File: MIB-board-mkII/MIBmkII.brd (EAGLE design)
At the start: 68.2 x 43.2 mm, 27 parts, among them IC1 74HC125N, X1 MAB5SH, X2 MAB5SH

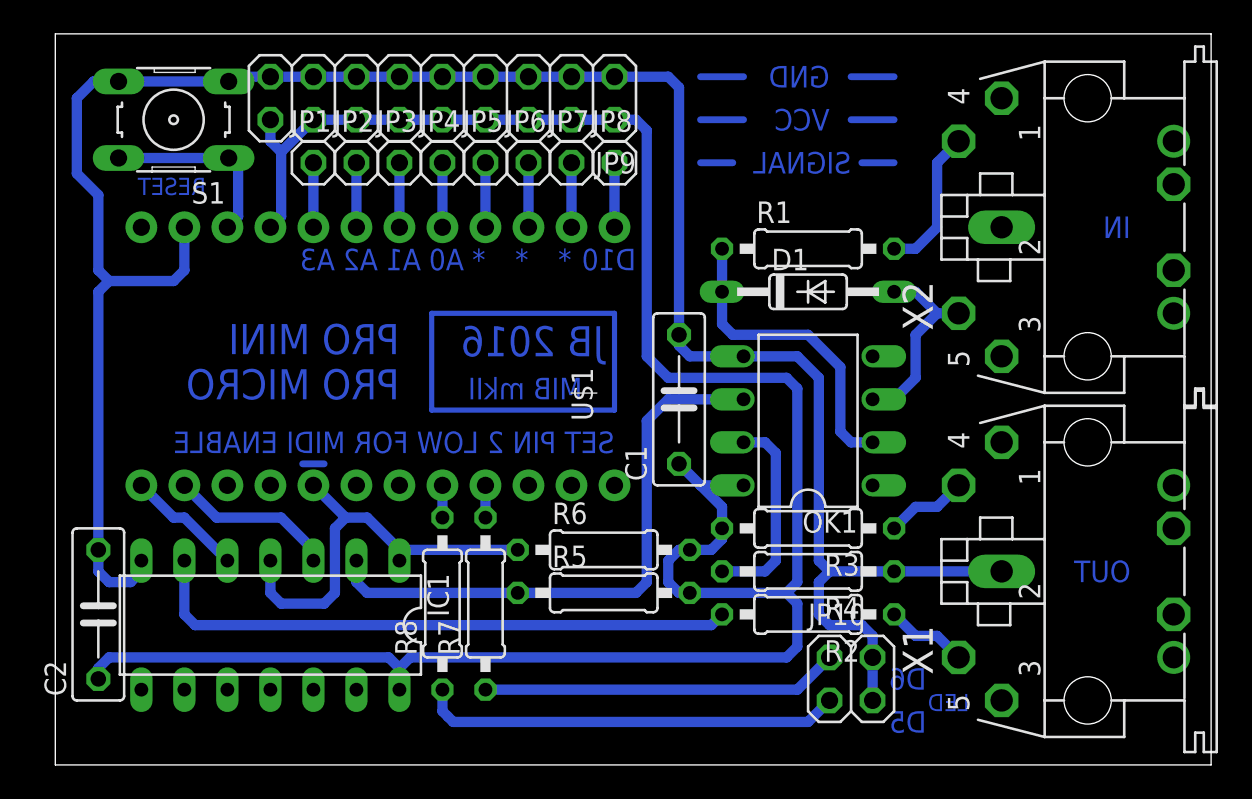
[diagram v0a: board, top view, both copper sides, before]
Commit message: Corrected labeling on silkscreen. Increased size of some pads and traces.
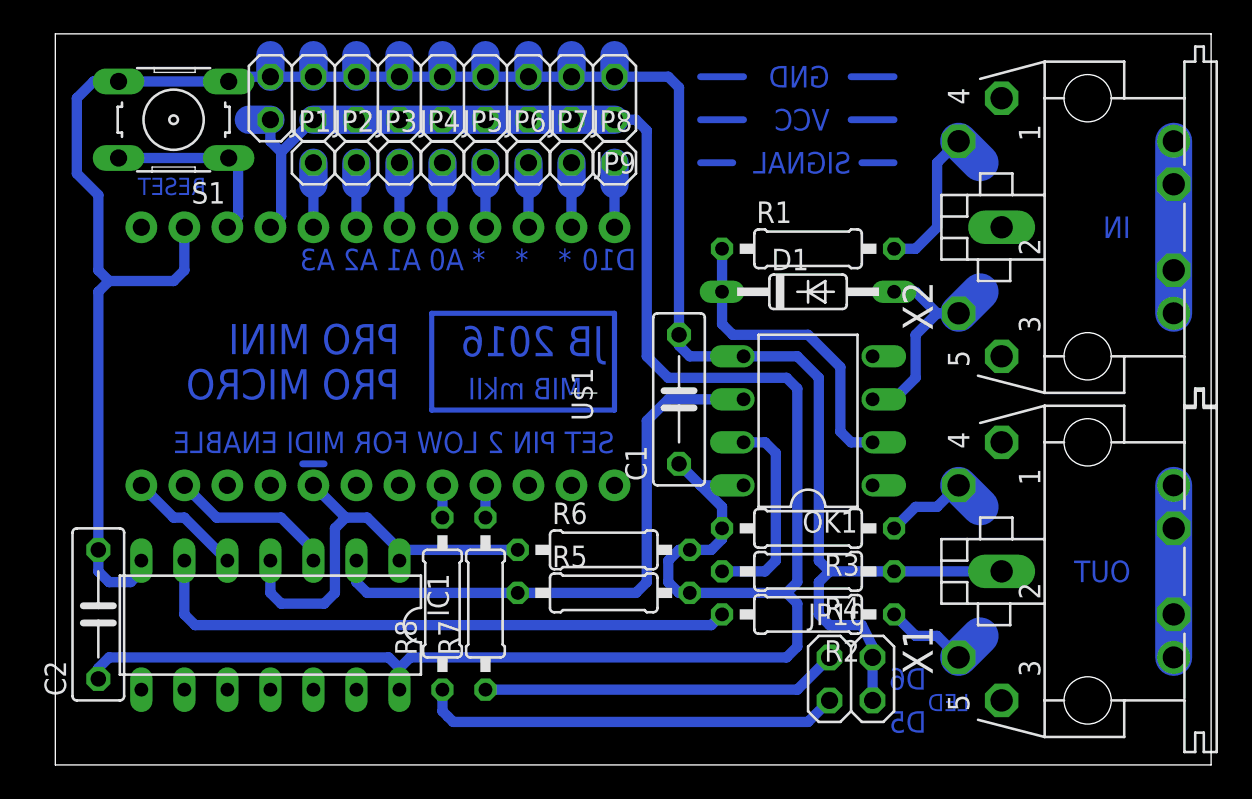
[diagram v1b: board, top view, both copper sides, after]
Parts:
- D1: value 1N4148DO35-10 -> 1N4148
- U$1: value ARDUINO_PRO_MICRO -> ARDUINO
- X1, X2: value MAB5SH -> (none)
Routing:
- net N$4: track 132.8 -> 151.8 mm
- net N$5: track 133.4 -> 144.8 mm
- net N$23: track 0.00 -> 10.2 mm, vias 1 -> 2
- net N$25: track 0.00 -> 10.2 mm, vias 1 -> 2
- net N$13: track 4.86 -> 6.66 mm
- net N$7: track 11.7 -> 13.5 mm
- net N$14: track 8.67 -> 10.5 mm
- net N$11: track 4.86 -> 6.66 mm
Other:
- board text added: "G"
- board text added: "S"
- board text added: "V"
